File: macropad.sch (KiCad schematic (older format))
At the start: 32 parts, among them SW1 Rotary_Encoder_Switch, SW2 SW_Push, U1 ProMicro

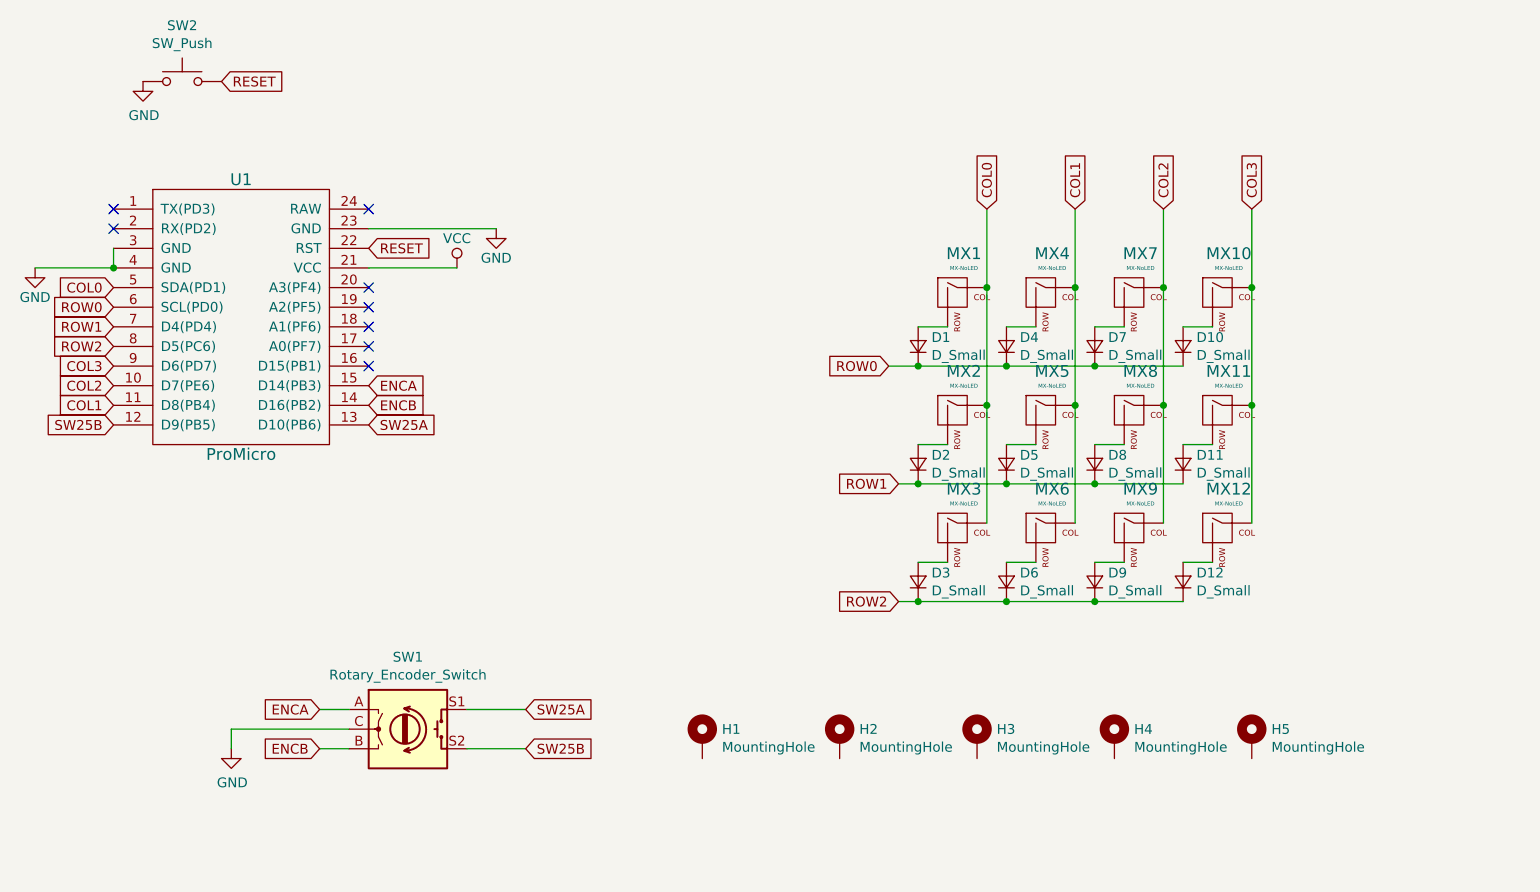
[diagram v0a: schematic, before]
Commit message: pcb overhaul
Added second rotary encoder
Moved Pro Micro under switches
Made backplate
Added artwork
Made pcb smaller overall
Added mousebites as symbol
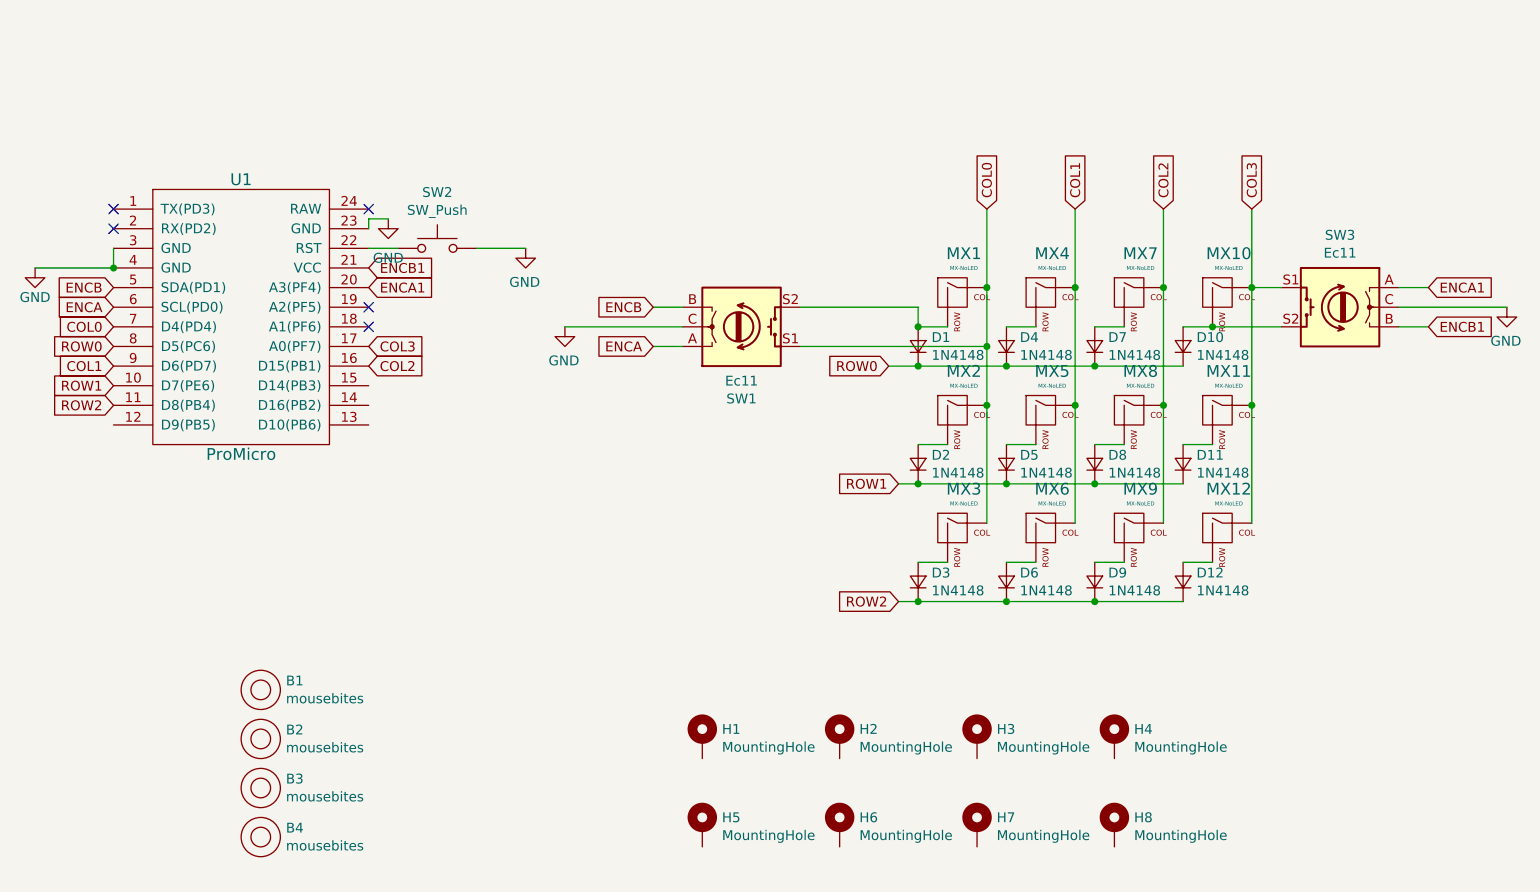
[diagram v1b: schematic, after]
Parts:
- removed H4: MountingHole, MountingHole:MountingHole_2.2mm_M2_Pad, symbol Mechanical:MountingHole_Pad
- added B1, B2, B3, B4: mousebites, random-keyboard-parts:breakaway-mousebites, symbol random-keyboard-parts:mousebites
- added H5, H6, H7, H8: MountingHole, MountingHole:MountingHole_2.2mm_M2_Pad, symbol Mechanical:MountingHole_Pad
- added SW3: Ec11, macropad:RotaryEncoder_Alps_EC11E-Switch_Vertical_H20mm, symbol Device:Rotary_Encoder_Switch
- D1, D10, D11, D12, D2, D3, D4, D5, D6, D7, D8, D9: value D_Small -> 1N4148
- SW1: value Rotary_Encoder_Switch -> Ec11
- renumbered H5 to H4
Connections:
- net COL0: now also SW1.S1, U1.7 (D4(PD4)); no longer U1.5 (SDA(PD1))
- net COL1: now also U1.9 (D6(PD7)); no longer U1.11 (D8(PB4))
- net COL2: now also U1.16 (D15(PB1)); no longer U1.10 (D7(PE6))
- net COL3: now also U1.17 (A0(PF7)), SW3.S1; no longer U1.9 (D6(PD7))
- net ENCA: now also U1.6 (SCL(PD0)); no longer U1.15 (D14(PB3))
- net ENCB: now also U1.5 (SDA(PD1)); no longer U1.14 (D16(PB2))
- net GND: now also SW3.C
- net ROW0: now also U1.8 (D5(PC6)); no longer U1.6 (SCL(PD0))
- net ROW1: now also U1.10 (D7(PE6)); no longer U1.7 (D4(PD4))
- net ROW2: now also U1.11 (D8(PB4)); no longer U1.8 (D5(PC6))
- net ENCA1: now reaches U1.20 (A3(PF4))
- net ENCA1: now also SW3.A
- net at D1.2 (A), MX1.2 (ROW): now also SW1.S2
- net at D10.2 (A), MX10.2 (ROW): now also SW3.S2
- net RESET: no longer names the net of SW2.2, U1.22 (RST)
- net SW25A: no longer names the net of U1.13 (D10(PB6))
- net SW25A: no longer SW1.S1
- net SW25B: no longer names the net of U1.12 (D9(PB5))
- net SW25B: no longer SW1.S2
- net VCC renamed ENCB1
- net ENCB1: now also SW3.B
- no-connect marks 8 -> 5
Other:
- moved on the sheet: H4, SW1, SW2

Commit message: Small fixes to PCB
Rotated rotary encoders 180*
Changed switch footprint to MX_Only
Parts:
- MX1, MX10, MX11, MX12, MX2, MX3, MX4, MX5, MX6, MX7, MX8, MX9: footprint MX_Alps_Hybrid:MX-1U-NoLED -> MX_Only:MXOnly-1U-NoLED
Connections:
- net COL0: now also SW1.S2, U1.9 (D6(PD7)); no longer SW1.S1, U1.7 (D4(PD4))
- net COL1: now also U1.10 (D7(PE6)); no longer U1.9 (D6(PD7))
- net COL3: now also SW3.S2; no longer SW3.S1
- net ENCA: now also U1.8 (D5(PC6)); no longer U1.6 (SCL(PD0))
- net ENCA1: now also U1.19 (A2(PF5)); no longer U1.20 (A3(PF4))
- net ENCB: now also U1.7 (D4(PD4)); no longer U1.5 (SDA(PD1))
- net ENCB1: now also U1.20 (A3(PF4)); no longer U1.21 (VCC)
- net ROW0: now also U1.18 (A1(PF6)); no longer U1.8 (D5(PC6))
- net ROW1: now also U1.11 (D8(PB4)); no longer U1.10 (D7(PE6))
- net ROW2: now also U1.12 (D9(PB5)); no longer U1.11 (D8(PB4))
- net at D1.2 (A), MX1.2 (ROW): now also SW1.S1; no longer SW1.S2
- net at D10.2 (A), MX10.2 (ROW): now also SW3.S1; no longer SW3.S2
- new net VCC: U1.21 (VCC)
- no-connect marks 5 -> 3
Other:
- moved on the sheet: B1, B2, B3, B4
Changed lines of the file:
@@
 Wire Wire Line
 	3950 2000 4100 2000
+Text GLabel 3950 2200 0    50   Input ~ 0
+ENCB
 Text GLabel 3950 2000 0    50   Input ~ 0
+ENCA
+Text GLabel 1200 2100 0    50   Input ~ 0
 ENCB
-Text GLabel 3950 2200 0    50   Input ~ 0
-ENCA
-Text GLabel 1200 1900 0    50   Input ~ 0
-ENCB
-Text GLabel 1200 2000 0    50   Input ~ 0
+Text GLabel 1200 2200 0    50   Input ~ 0
 ENCA
 Wire Wire Line
@@
 $EndComp
 NoConn ~ 2500 1500
-Text GLabel 1200 2100 0    50   Input ~ 0
+Text GLabel 1200 2300 0    50   Input ~ 0
 COL0
 $Comp
@@
 Text GLabel 5150 2300 0    50   Input ~ 0
 ROW0
-Text GLabel 1200 2300 0    50   Input ~ 0
+Text GLabel 1200 2400 0    50   Input ~ 0
 COL1
 Text GLabel 2500 2300 2    50   Input ~ 0
@@
 F 0 "MX1" H 5533 2173 60  0000 C CNN
 F 1 "MX-NoLED" H 5533 2099 20  0000 C CNN
-F 2 "MX_Alps_Hybrid:MX-1U-NoLED" H 4875 1925 60  0001 C CNN
+F 2 "MX_Only:MXOnly-1U-NoLED" H 4875 1925 60  0001 C CNN
 F 3 "" H 4875 1925 60  0001 C CNN
 	1    5500 1950
@@
 F 0 "MX4" H 5983 2173 60  0000 C CNN
 F 1 "MX-NoLED" H 5983 2099 20  0000 C CNN
-F 2 "MX_Alps_Hybrid:MX-1U-NoLED" H 5325 1925 60  0001 C CNN
+F 2 "MX_Only:MXOnly-1U-NoLED" H 5325 1925 60  0001 C CNN
 F 3 "" H 5325 1925 60  0001 C CNN
 	1    5950 1950
@@
 F 0 "MX7" H 6433 2173 60  0000 C CNN
 F 1 "MX-NoLED" H 6433 2099 20  0000 C CNN
-F 2 "MX_Alps_Hybrid:MX-1U-NoLED" H 5775 1925 60  0001 C CNN
+F 2 "MX_Only:MXOnly-1U-NoLED" H 5775 1925 60  0001 C CNN
 F 3 "" H 5775 1925 60  0001 C CNN
 	1    6400 1950
@@
 F 0 "MX10" H 6883 2173 60  0000 C CNN
 F 1 "MX-NoLED" H 6883 2099 20  0000 C CNN
-F 2 "MX_Alps_Hybrid:MX-1U-NoLED" H 6225 1925 60  0001 C CNN
+F 2 "MX_Only:MXOnly-1U-NoLED" H 6225 1925 60  0001 C CNN
 F 3 "" H 6225 1925 60  0001 C CNN
 	1    6850 1950
@@
 F 0 "MX2" H 5533 2773 60  0000 C CNN
 F 1 "MX-NoLED" H 5533 2699 20  0000 C CNN
-F 2 "MX_Alps_Hybrid:MX-1U-NoLED" H 4875 2525 60  0001 C CNN
+F 2 "MX_Only:MXOnly-1U-NoLED" H 4875 2525 60  0001 C CNN
 F 3 "" H 4875 2525 60  0001 C CNN
 	1    5500 2550
@@
 F 0 "MX5" H 5983 2773 60  0000 C CNN
 F 1 "MX-NoLED" H 5983 2699 20  0000 C CNN
-F 2 "MX_Alps_Hybrid:MX-1U-NoLED" H 5325 2525 60  0001 C CNN
+F 2 "MX_Only:MXOnly-1U-NoLED" H 5325 2525 60  0001 C CNN
 F 3 "" H 5325 2525 60  0001 C CNN
 	1    5950 2550
@@
 F 0 "MX8" H 6433 2773 60  0000 C CNN
 F 1 "MX-NoLED" H 6433 2699 20  0000 C CNN
-F 2 "MX_Alps_Hybrid:MX-1U-NoLED" H 5775 2525 60  0001 C CNN
+F 2 "MX_Only:MXOnly-1U-NoLED" H 5775 2525 60  0001 C CNN
 F 3 "" H 5775 2525 60  0001 C CNN
 	1    6400 2550
@@
 F 0 "MX11" H 6883 2773 60  0000 C CNN
 F 1 "MX-NoLED" H 6883 2699 20  0000 C CNN
-F 2 "MX_Alps_Hybrid:MX-1U-NoLED" H 6225 2525 60  0001 C CNN
+F 2 "MX_Only:MXOnly-1U-NoLED" H 6225 2525 60  0001 C CNN
 F 3 "" H 6225 2525 60  0001 C CNN
 	1    6850 2550
@@
 F 0 "MX3" H 5533 3373 60  0000 C CNN
 F 1 "MX-NoLED" H 5533 3299 20  0000 C CNN
-F 2 "MX_Alps_Hybrid:MX-1U-NoLED" H 4875 3125 60  0001 C CNN
+F 2 "MX_Only:MXOnly-1U-NoLED" H 4875 3125 60  0001 C CNN
 F 3 "" H 4875 3125 60  0001 C CNN
 	1    5500 3150
@@
 F 0 "MX6" H 5983 3373 60  0000 C CNN
 F 1 "MX-NoLED" H 5983 3299 20  0000 C CNN
-F 2 "MX_Alps_Hybrid:MX-1U-NoLED" H 5325 3125 60  0001 C CNN
+F 2 "MX_Only:MXOnly-1U-NoLED" H 5325 3125 60  0001 C CNN
 F 3 "" H 5325 3125 60  0001 C CNN
 	1    5950 3150
@@
 F 0 "MX9" H 6433 3373 60  0000 C CNN
 F 1 "MX-NoLED" H 6433 3299 20  0000 C CNN
-F 2 "MX_Alps_Hybrid:MX-1U-NoLED" H 5775 3125 60  0001 C CNN
+F 2 "MX_Only:MXOnly-1U-NoLED" H 5775 3125 60  0001 C CNN
 F 3 "" H 5775 3125 60  0001 C CNN
 	1    6400 3150
@@
 F 0 "MX12" H 6883 3373 60  0000 C CNN
 F 1 "MX-NoLED" H 6883 3299 20  0000 C CNN
-F 2 "MX_Alps_Hybrid:MX-1U-NoLED" H 6225 3125 60  0001 C CNN
+F 2 "MX_Only:MXOnly-1U-NoLED" H 6225 3125 60  0001 C CNN
 F 3 "" H 6225 3125 60  0001 C CNN
 	1    6850 3150
@@
 	-1   0    0    -1
 $EndComp
-Text GLabel 1200 2200 0    50   Input ~ 0
+Text GLabel 2500 2100 2    50   Input ~ 0
 ROW0
-Text GLabel 1200 2400 0    50   Input ~ 0
+Text GLabel 1200 2500 0    50   Input ~ 0
 ROW1
-Text GLabel 1200 2500 0    50   Input ~ 0
+Text GLabel 1200 2600 0    50   Input ~ 0
 ROW2
 NoConn ~ 1200 1500
@@
 Wire Wire Line
 	800  1800 1200 1800
-NoConn ~ 2500 2000
-NoConn ~ 2500 2100
 Wire Wire Line
 	3050 1700 3300 1700
@@
 Wire Wire Line
 	7900 2100 7750 2100
+Text GLabel 7900 1900 2    50   Input ~ 0
+ENCB1
 Text GLabel 7900 2100 2    50   Input ~ 0
-ENCB1
-Text GLabel 7900 1900 2    50   Input ~ 0
 ENCA1
 Wire Wire Line
@@
 F 3 "~" H 7450 2260 50  0001 C CNN
 	1    7450 2000
-	-1   0    0    -1
+	-1   0    0    1
 $EndComp
 $Comp
@@
 F 3 "~" H 4400 2360 50  0001 C CNN
 	1    4400 2100
-	1    0    0    1
+	1    0    0    -1
 $EndComp
 Wire Wire Line
 	7750 2000 8300 2000
-Text GLabel 2500 1800 2    50   Input ~ 0
+Text GLabel 2500 1900 2    50   Input ~ 0
 ENCB1
-Text GLabel 2500 1900 2    50   Input ~ 0
+Text GLabel 2500 2000 2    50   Input ~ 0
 ENCA1
 Connection ~ 1200 1800
@@
 L random-keyboard-parts:mousebites B1
 U 1 1 600A1F74
-P 1950 3950
-F 0 "B1" H 2078 3996 50  0000 L CNN
-F 1 "mousebites" H 2078 3905 50  0000 L CNN
-F 2 "random-keyboard-parts:breakaway-mousebites" H 1950 3950 50  0001 C CNN
-F 3 "" H 1950 3950 50  0001 C CNN
-	1    1950 3950
+P 800 4050
+F 0 "B1" H 928 4096 50  0000 L CNN
+F 1 "mousebites" H 928 4005 50  0000 L CNN
+F 2 "random-keyboard-parts:breakaway-mousebites" H 800 4050 50  0001 C CNN
+F 3 "" H 800 4050 50  0001 C CNN
+	1    800  4050
 	1    0    0    -1
 $EndComp
@@
 L random-keyboard-parts:mousebites B2
 U 1 1 600A403F
-P 1950 4200
-F 0 "B2" H 2078 4246 50  0000 L CNN
-F 1 "mousebites" H 2078 4155 50  0000 L CNN
-F 2 "random-keyboard-parts:breakaway-mousebites" H 1950 4200 50  0001 C CNN
-F 3 "" H 1950 4200 50  0001 C CNN
-	1    1950 4200
+P 800 4300
+F 0 "B2" H 928 4346 50  0000 L CNN
+F 1 "mousebites" H 928 4255 50  0000 L CNN
+F 2 "random-keyboard-parts:breakaway-mousebites" H 800 4300 50  0001 C CNN
+F 3 "" H 800 4300 50  0001 C CNN
+	1    800  4300
 	1    0    0    -1
 $EndComp
@@
 L random-keyboard-parts:mousebites B3
 U 1 1 600A4898
-P 1950 4450
-F 0 "B3" H 2078 4496 50  0000 L CNN
-F 1 "mousebites" H 2078 4405 50  0000 L CNN
-F 2 "random-keyboard-parts:breakaway-mousebites" H 1950 4450 50  0001 C CNN
-F 3 "" H 1950 4450 50  0001 C CNN
-	1    1950 4450
+P 800 4550
+F 0 "B3" H 928 4596 50  0000 L CNN
+F 1 "mousebites" H 928 4505 50  0000 L CNN
+F 2 "random-keyboard-parts:breakaway-mousebites" H 800 4550 50  0001 C CNN
+F 3 "" H 800 4550 50  0001 C CNN
+	1    800  4550
 	1    0    0    -1
 $EndComp
@@
 L random-keyboard-parts:mousebites B4
 U 1 1 600A5097
-P 1950 4700
-F 0 "B4" H 2078 4746 50  0000 L CNN
-F 1 "mousebites" H 2078 4655 50  0000 L CNN
-F 2 "random-keyboard-parts:breakaway-mousebites" H 1950 4700 50  0001 C CNN
-F 3 "" H 1950 4700 50  0001 C CNN
-	1    1950 4700
+P 800 4800
+F 0 "B4" H 928 4846 50  0000 L CNN
+F 1 "mousebites" H 928 4755 50  0000 L CNN
+F 2 "random-keyboard-parts:breakaway-mousebites" H 800 4800 50  0001 C CNN
+F 3 "" H 800 4800 50  0001 C CNN
+	1    800  4800
 	1    0    0    -1
 $EndComp
@@
 	1    0    0    -1
 $EndComp
+$Comp
+L power:VCC #PWR0106
+U 1 1 600BE27B
+P 2850 1800
+F 0 "#PWR0106" H 2850 1650 50  0001 C CNN
+F 1 "VCC" H 2867 1973 50  0000 C CNN
+F 2 "" H 2850 1800 50  0001 C CNN
+F 3 "" H 2850 1800 50  0001 C CNN
+	1    2850 1800
+	1    0    0    -1
+$EndComp
+Wire Wire Line
+	2500 1800 2850 1800
 $EndSCHEMATC

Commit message: Changed diode placement
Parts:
- SW2: footprint macropad:TACT_SWITCH_TVBP06 -> random-keyboard-parts:Jumper-UserFriendly-Small
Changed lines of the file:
@@
 F 0 "SW2" H 2850 1985 50  0000 C CNN
 F 1 "SW_Push" H 2850 1894 50  0000 C CNN
-F 2 "macropad:TACT_SWITCH_TVBP06" H 2850 1900 50  0001 C CNN
+F 2 "random-keyboard-parts:Jumper-UserFriendly-Small" H 2850 1900 50  0001 C CNN
 F 3 "~" H 2850 1900 50  0001 C CNN
 	1    2850 1700
